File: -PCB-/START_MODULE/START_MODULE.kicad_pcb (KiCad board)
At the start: 4 copper layers, 15 x 13 mm, 6 parts, among them J1 Conn_01x03_Pin, J2 Conn_01x04_Pin, U1 ATtiny85-20S, U2 TSOP382xx

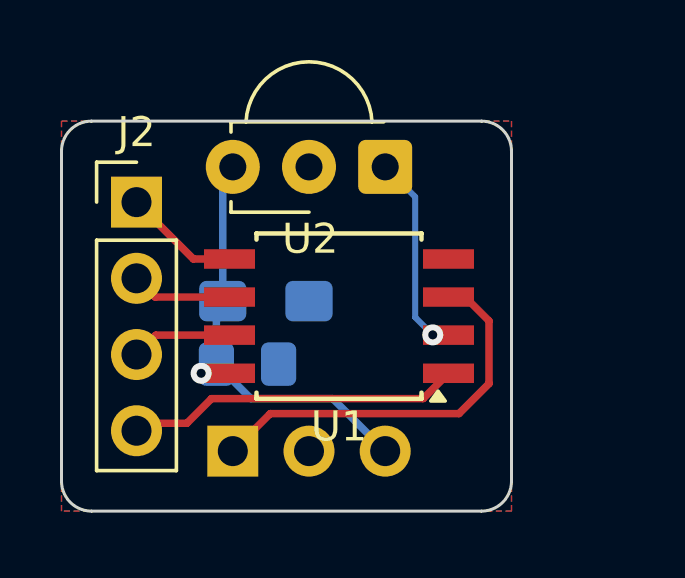
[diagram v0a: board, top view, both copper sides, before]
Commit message: Silkscreen update IR module
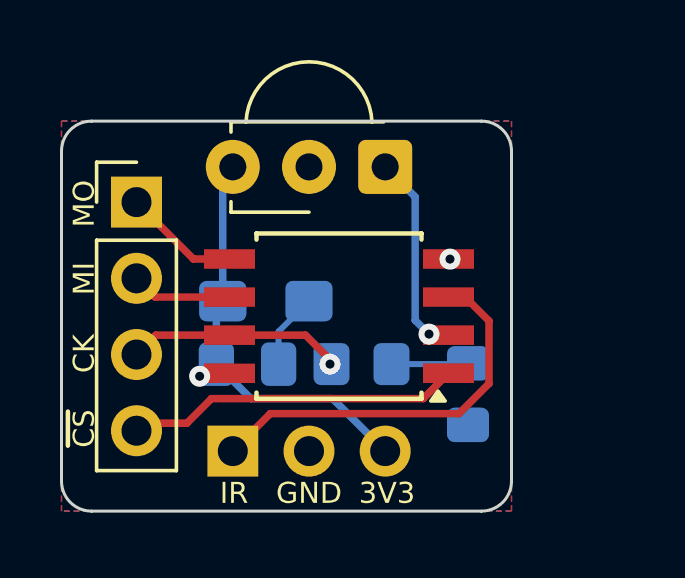
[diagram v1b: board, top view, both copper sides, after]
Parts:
- added D1: LED, LED_SMD:LED_0805_2012Metric_Pad1.15x1.40mm_HandSolder, B.Cu at (150.3, 102.6)
- added R1: 100R, Resistor_SMD:R_0805_2012Metric_Pad1.20x1.40mm_HandSolder, B.Cu at (146.8, 101.6)
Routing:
- net /SCK: track 3.62 -> 7.38 mm, vias 0 -> 1
- net Net-(D1-A): track 0.00 -> 2.82 mm
- net GND: track 0.00 -> 2.66 mm, vias 0 -> 1
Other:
- board text added: "3V3"
- board text added: "CK"
- board text added: "GND"
- board text added: "IR"
- board text added: "MI"
- board text added: "MO"
- board text added: "~{CS}"

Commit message: IR_module update
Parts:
- added D2: LED, LED_SMD:LED_0805_2012Metric_Pad1.15x1.40mm_HandSolder, F.Cu at (139.2, 95.0)
- added R2: 10k, Resistor_SMD:R_0805_2012Metric_Pad1.20x1.40mm_HandSolder, B.Cu at (148.2, 101.5)
- added R3: 220R, Resistor_SMD:R_0805_2012Metric_Pad1.20x1.40mm_HandSolder, B.Cu at (139.2, 95.0)
- added SW1: SW_Push, sumec_brd:SW_SPST_EVQPE1, F.Cu at (139.2, 100.0)
- D1: moved to F.Cu
- R1: value 100R -> 220R
- moved J2 13.5 mm to (152.8, 96.0)
- moved D1 11.3 mm to (139.2, 105.0), turned to 0 degrees
- moved R1 8.23 mm to (139.2, 105.0)
- moved C2 1.55 mm to (144.5, 101.5)
- moved C1 1.54 mm to (145.1, 99.4)
- moved J1 1.02 mm to (143.5, 104.4)
- moved U2 1.00 mm to (148.5, 95.0)
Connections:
- R1 pad 1: /SCK -> /MISO
- U1 pad 2: IR_OUT -> IR_DECODED
- U1 pad 3: IR_DECODED -> IR_INPUT
- U2 pad 1: IR_OUT -> IR_INPUT
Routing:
- net /MISO: track 3.61 -> 19.7 mm, vias 0 -> 1
- net /MOSI: track 4.13 -> 16.7 mm, vias 0 -> 1
- net GND: track 2.66 -> 12.7 mm, vias 1 -> 2
- net IR_OUT: track 6.18 -> 0.00 mm, vias 1 -> 0
- net IR_INPUT: track 0.00 -> 4.97 mm, vias 0 -> 1
- net /~{CS}: track 11.1 -> 15.2 mm, vias 0 -> 1
- net /SCK: track 7.38 -> 11.4 mm
- net Net-(D1-A): track 2.82 -> 0.03 mm, vias 0 -> 1
- net +3.3V: track 14.6 -> 17.1 mm, vias 1 -> 2
- net IR_DECODED: track 13.2 -> 11.3 mm
- net Net-(D2-A): vias 0 -> 1
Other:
- board size 15 x 13 mm -> 18.5 x 13 mm
- copper layers 4 -> 2
